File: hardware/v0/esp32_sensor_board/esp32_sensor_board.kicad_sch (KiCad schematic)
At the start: 0 parts

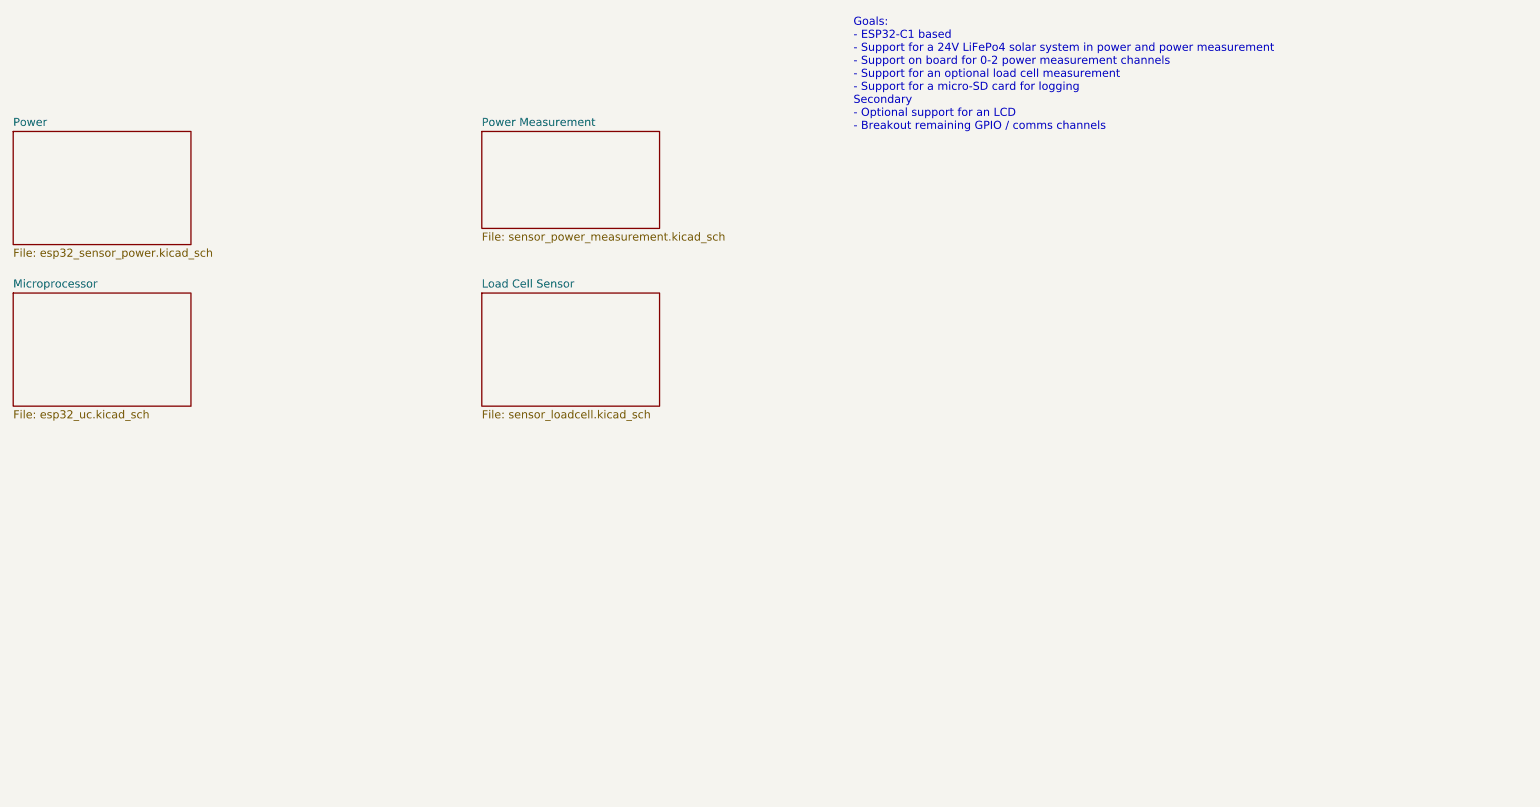
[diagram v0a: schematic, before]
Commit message: PCB ordered, a few initial mistakes fixed
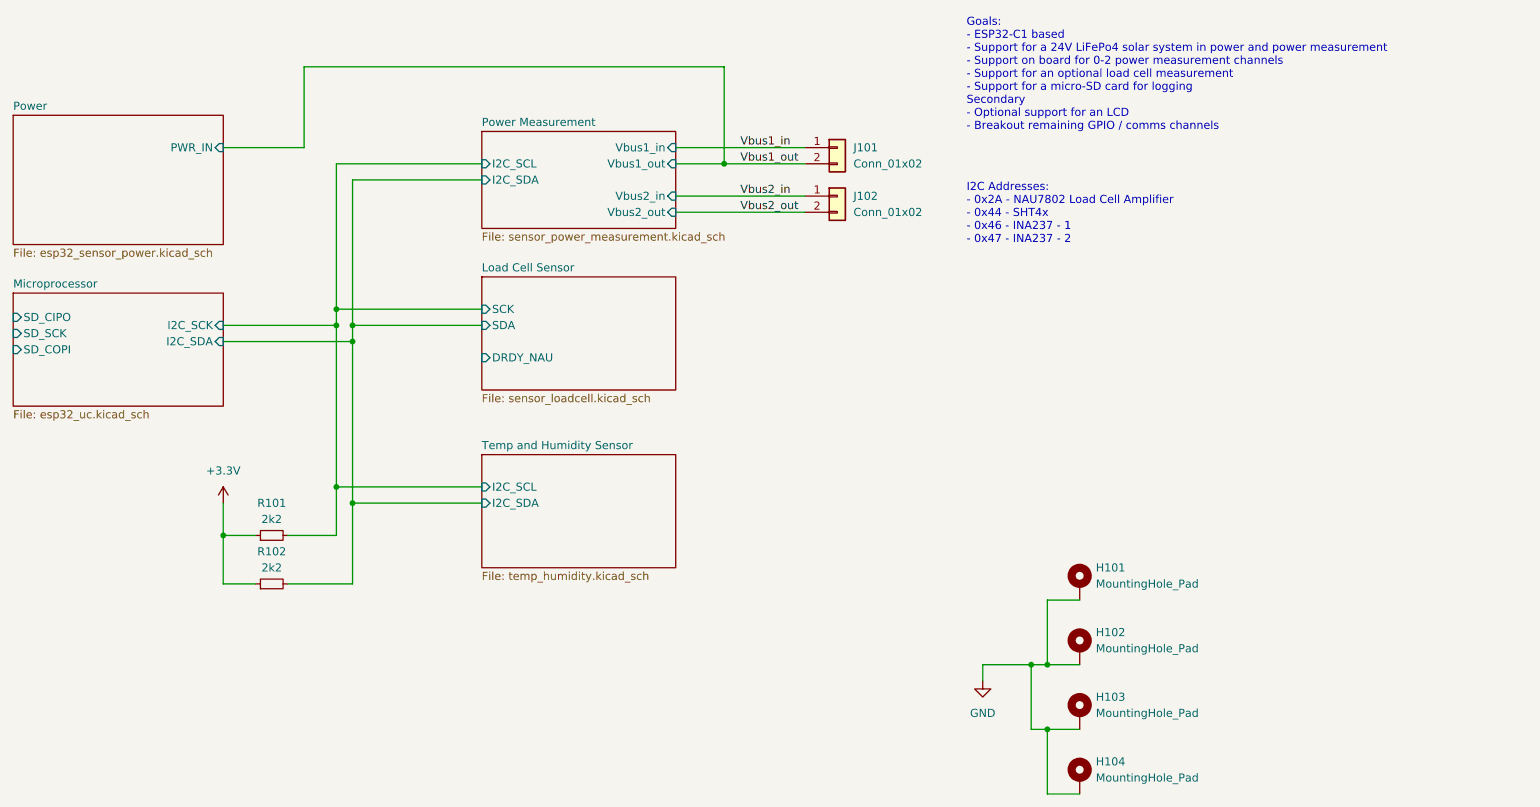
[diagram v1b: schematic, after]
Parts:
- added H101, H102, H103, H104: MountingHole_Pad, MountingHole:MountingHole_3.2mm_M3_DIN965_Pad, symbol Mechanical:MountingHole_Pad
- added J101, J102: Conn_01x02, Connector_Phoenix_MSTB:PhoenixContact_MSTBA_2,5_2-G-5,08_1x02_P5.08mm_Horizontal, symbol Connector_Generic:Conn_01x02
- added R101, R102: 2k2, Resistor_SMD:R_0603_1608Metric, symbol Device:R_Small
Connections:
- new net +3.3V: R101.1, R102.1
- new net GND: H101.1, H102.1, H103.1, H104.1
- new net Load Cell Sensor/SCK: R101.2
- new net Load Cell Sensor/SDA: R102.2
- new net Vbus1_in: J101.1 (Pin_1)
- new net Vbus1_out: J101.2 (Pin_2)
- new net Vbus2_in: J102.1 (Pin_1)
- new net Vbus2_out: J102.2 (Pin_2)
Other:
- added sheet Temp and Humidity Sensor (temp_humidity.kicad_sch)
- sheet Load Cell Sensor ports: added DRDY_NAU, SCK, SDA; removed none
- sheet Microprocessor ports: added I2C_SCK, I2C_SDA, SD_CIPO, SD_COPI, SD_SCK; removed none
- sheet Power ports: added PWR_IN; removed none
- sheet Power Measurement ports: added I2C_SCL, I2C_SDA, Vbus1_in, Vbus1_out, Vbus2_in, Vbus2_out; removed none
- note added: "I2C Addresses: - 0x2A - NAU7802 Load Cell Amplifier - 0x44 - SHT4x - 0x46 - INA237 - 1 - 0x47 - INA237 - 2"

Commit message: Board refactor WIP.  Still needs PU resistors
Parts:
- added J103, J104: Conn_01x02, Connector_Phoenix_MSTB:PhoenixContact_MSTBA_2,5_2-G-5,08_1x02_P5.08mm_Horizontal, symbol Connector_Generic:Conn_01x02
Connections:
- net GND: now also J101.1 (Pin_1), J102.2 (Pin_2), J103.1 (Pin_1), J104.2 (Pin_2)
- net Vbus1_in: now also J101.2 (Pin_2); no longer J101.1 (Pin_1)
- net Vbus1_out: now also J102.1 (Pin_1); no longer J101.2 (Pin_2)
- net Vbus2_in: now also J103.2 (Pin_2); no longer J102.1 (Pin_1)
- net Vbus2_out: now also J104.1 (Pin_1); no longer J102.2 (Pin_2)
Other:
- sheet Microprocessor ports: added GPIO7, SPI_CIPO, SPI_COPI, SPI_CS1, SPI_SCK, VIN; removed SD_CIPO, SD_COPI, SD_SCK
- note added: "I2C Addresses: - 0x2A - NAU7802 Load Cell Amplifier - 0x44 - SHT4x - 0x46 - INA237 - 1 0x45 on prototype board after modification - 0x47 - INA237 - 2"
- note removed: "I2C Addresses: - 0x2A - NAU7802 Load Cell Amplifier - 0x44 - SHT4x - 0x46 - INA237 - 1 - 0x47 - INA237 - 2"
- moved on the sheet: J101, J102

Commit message: TVS and PU work
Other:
- sheet Microprocessor ports: added DATA_READY; removed GPIO7
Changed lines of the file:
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@@
-      (effects (font (size 1.27 1.27)) (justify right))
-    )
-    (pin "GPIO7" input (at 86.36 71.12 0)
       (effects (font (size 1.27 1.27)) (justify right))
     )
@@
       (effects (font (size 1.27 1.27)) (justify right))
     )
+    (pin "DATA_READY" input (at 86.36 71.12 0)
+      (effects (font (size 1.27 1.27)) (justify right))
+    )
